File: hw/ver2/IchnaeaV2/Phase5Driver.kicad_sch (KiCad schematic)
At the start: 21 parts, among them Q2 MCAC80N10Y, Q3 MCAC80N10Y, Q4 MCAC80N10Y, Q5 MCAC80N10Y, U2 HIP2210

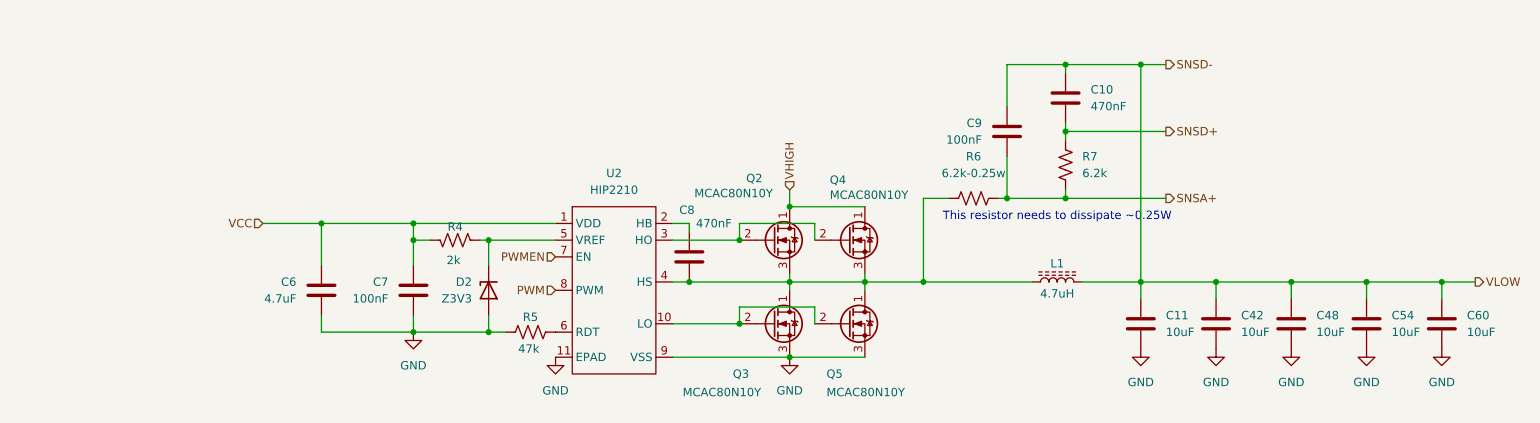
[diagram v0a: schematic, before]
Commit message: Trying to further compress power loop area
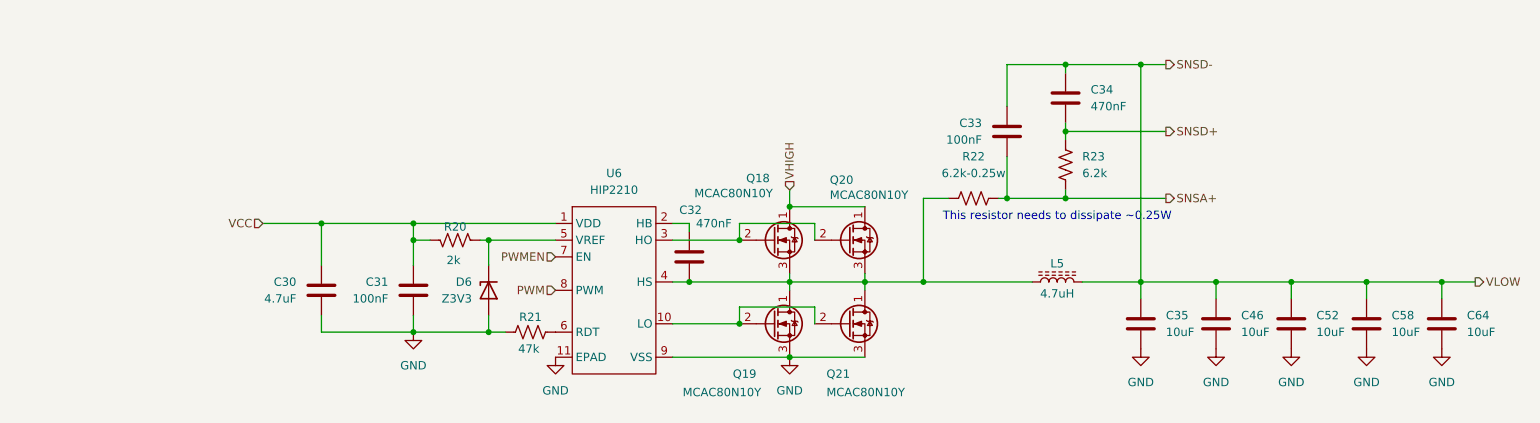
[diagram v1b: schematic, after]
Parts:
- renumbered C6 to C30, C7 to C31, C8 to C32, C9 to C33, C10 to C34, C11 to C35, C42 to C46, C48 to C52, C54 to C58, C60 to C64, D2 to D6, L1 to L5, Q2 to Q18, Q3 to Q19, Q4 to Q20, Q5 to Q21, R4 to R20, R5 to R21, R6 to R22, R7 to R23, U2 to U6

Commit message: Not quite happy with the power stage just yet.
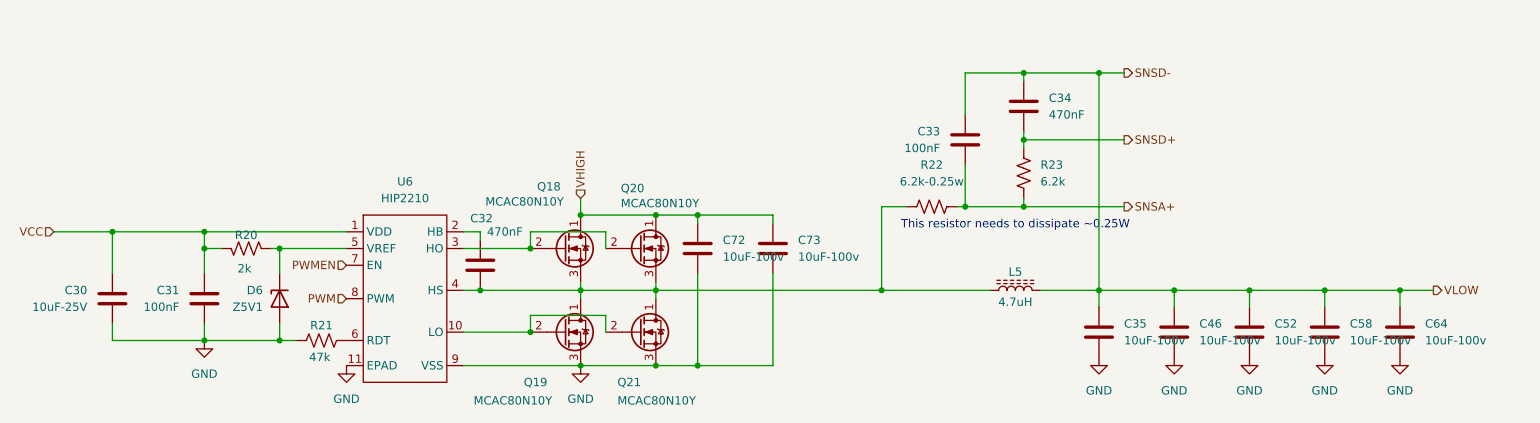
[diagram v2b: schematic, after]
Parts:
- added C72, C73: 10uF-100v, Capacitor_SMD:C_1210_3225Metric_Pad1.33x2.70mm_HandSolder, symbol Device:C
- C30: value 4.7uF -> 10uF-25V; LCSC C19666 -> C96446
- C35, C46, C52, C58, C64: value 10uF -> 10uF-100v
- D6: value Z3V3 -> Z5V1; LCSC C5353025 -> C2903912
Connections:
- net GND: now also C72.2, C73.2
- net VHIGH: now also C72.1, C73.1
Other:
- moved on the sheet: C30, C31, C32, C33, C34, C35, C46, C52, C58, C64, D6, L5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

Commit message: Sync work to main PC
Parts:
- removed C31: 100nF, Capacitor_SMD:C_0603_1608Metric, symbol Device:C
- removed D6: Z5V1, Diode_SMD:D_SOD-123, symbol Device:D_Zener
- removed R20: 2k, Resistor_SMD:R_0603_1608Metric, symbol Device:R_US
- added R62, R63: 0, Resistor_SMD:R_0603_1608Metric, symbol Device:R_US
- added R64: 10k, Resistor_SMD:R_0603_1608Metric, symbol Device:R_US
- added R65: 6.2k, Resistor_SMD:R_0603_1608Metric, symbol Device:R_US
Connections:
- net GND: now also R65.2
- net PWM: now also R63.2; no longer U6.8 (PWM)
- net PWMEN: now also R62.2; no longer U6.7 (EN)
- net SNSD-: now also L5.1; no longer L5.2
- net VCC: now also R64.1
- net at C32.2, Q18.3 (S), Q19.1 (D)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: now also L5.2; no longer L5.1
- net at U6.5 (VREF): now also R64.2, R65.1
- new net: R62.1, U6.7 (EN)
- new net: R63.1, U6.8 (PWM)
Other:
- moved on the sheet: C30, L5

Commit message: More power stage layout
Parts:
- removed C52: 10uF-100v, Capacitor_SMD:C_1210_3225Metric_Pad1.33x2.70mm_HandSolder, symbol Device:C
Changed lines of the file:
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@@
-	)
-	(junction
-		(at 232.41 96.52)
-		(diameter 0)
-		(color 0 0 0 0)
 	)
 	(junction
@@
 	(wire
 		(pts
-			(xy 232.41 96.52) (xy 232.41 99.06)
-		)
-		(stroke
-			(width 0)
-			(type default)
-		)
-	)
-	(wire
-		(pts
 			(xy 209.55 63.5) (xy 198.12 63.5)
 		)
@@
 	(wire
 		(pts
-			(xy 232.41 96.52) (xy 243.84 96.52)
+			(xy 220.98 96.52) (xy 243.84 96.52)
 		)
 		(stroke
@@
 		(pts
 			(xy 113.03 90.17) (xy 123.19 90.17)
-		)
-		(stroke
-			(width 0)
-			(type default)
-		)
-	)
-	(wire
-		(pts
-			(xy 220.98 96.52) (xy 232.41 96.52)
 		)
 		(stroke
@@
 	)
 	(symbol
-		(lib_id "Device:C")
-		(at 232.41 102.87 0)
-		(unit 1)
-		(exclude_from_sim no)
-		(in_bom yes)
-		(on_board yes)
-		(dnp no)
-		(fields_autoplaced yes)
-		(property "Reference" "C52"
-			(at 236.22 101.5999 0)
-			(effects
-				(font
-					(size 1.27 1.27)
-				)
-				(justify left)
-			)
-		)
-		(property "Value" "10uF-100v"
-			(at 236.22 104.1399 0)
-			(effects
-				(font
-					(size 1.27 1.27)
-				)
-				(justify left)
-			)
-		)
-		(property "Footprint" "Capacitor_SMD:C_1210_3225Metric_Pad1.33x2.70mm_HandSolder"
-			(at 233.3752 106.68 0)
-			(effects
-				(font
-					(size 1.27 1.27)
-				)
-				(hide yes)
-			)
-		)
-		(property "Datasheet" "~"
-			(at 232.41 102.87 0)
-			(effects
-				(font
-					(size 1.27 1.27)
-				)
-				(hide yes)
-			)
-		)
-		(property "Description" "Unpolarized capacitor"
-			(at 232.41 102.87 0)
-			(effects
-				(font
-					(size 1.27 1.27)
-				)
-				(hide yes)
-			)
-		)
-		(property "Field-1" ""
-			(at 232.41 102.87 0)
-			(effects
-				(font
-					(size 1.27 1.27)
-				)
-				(hide yes)
-			)
-		)
-		(property "Digikey" "445-CGA6P1X7R1N106M250ACCT-ND"
-			(at 232.41 102.87 0)
-			(effects
-				(font
-					(size 1.27 1.27)
-				)
-				(hide yes)
-			)
-		)
-		(property "LCSC" "C576517"
-			(at 232.41 102.87 0)
-			(effects
-				(font
-					(size 1.27 1.27)
-				)
-				(hide yes)
-			)
-		)
-		(pin "1"
-		)
-		(pin "2"
-		)
-		(instances
-			(project "IchnaeaV2"
-				(path "/93408532-1ffa-463d-873c-16289d2b7987/31a930eb-86fc-490d-aa2b-31b72c4dd29d/54a63e50-1efe-4308-b876-98aee26e8c6e"
-					(reference "C52")
-					(unit 1)
-				)
-			)
-		)
-	)
-	(symbol
 		(lib_id "Device:L_Ferrite")
 		(at 196.85 96.52 270)
@@
 					(unit 1)
 				)
-			)
-		)
-	)
-	(symbol
-		(lib_id "power:GND")
-		(at 232.41 106.68 0)
-		(unit 1)
-		(exclude_from_sim no)
-		(in_bom yes)
-		(on_board yes)
-		(dnp no)
-		(fields_autoplaced yes)
-		(property "Reference" "#PWR078"
-			(at 232.41 113.03 0)
-			(effects
-				(font
-					(size 1.27 1.27)
-				)
-				(hide yes)
-			)
-		)
-		(property "Value" "GND"
-			(at 232.41 111.76 0)
-			(effects
-				(font
-					(size 1.27 1.27)
-				)
-			)
-		)
-		(property "Footprint" ""
-			(at 232.41 106.68 0)
-			(effects
-				(font
-					(size 1.27 1.27)
-				)
-				(hide yes)
-			)
-		)
-		(property "Datasheet" ""
-			(at 232.41 106.68 0)
-			(effects
-				(font
-					(size 1.27 1.27)
-				)
-				(hide yes)
-			)
-		)
-		(property "Description" "Power symbol creates a global label with name \"GND\" , ground"
-			(at 232.41 106.68 0)
-			(effects
-				(font
-					(size 1.27 1.27)
-				)
-				(hide yes)
-			)
-		)
-		(pin "1"
-		)
-		(instances
-			(project "IchnaeaV2"
-				(path "/93408532-1ffa-463d-873c-16289d2b7987/31a930eb-86fc-490d-aa2b-31b72c4dd29d/54a63e50-1efe-4308-b876-98aee26e8c6e"
-					(reference "#PWR078")
-					(unit 1)
-				)

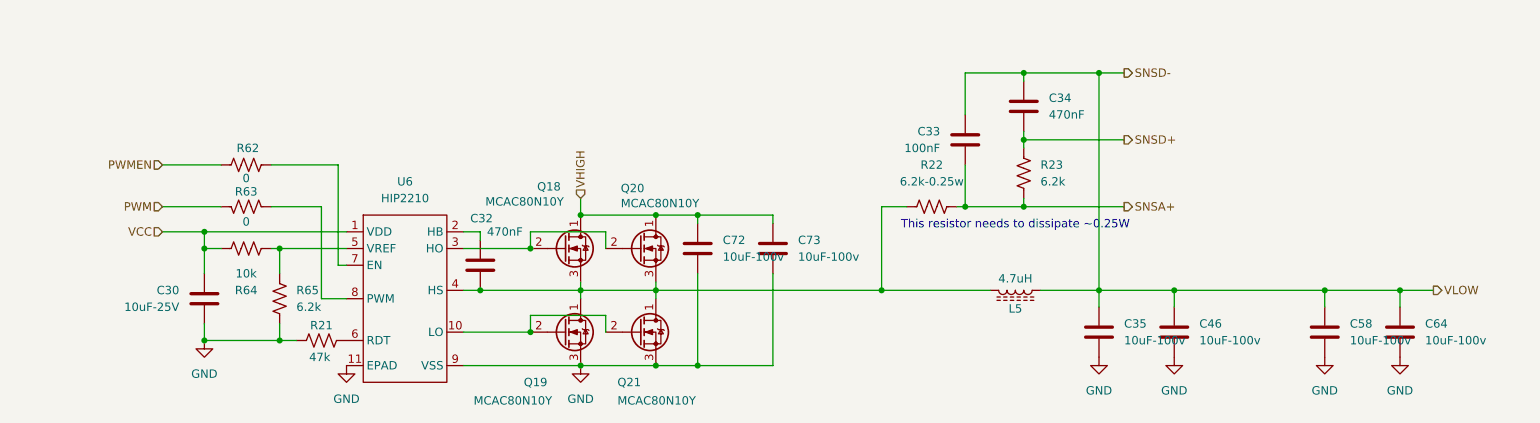
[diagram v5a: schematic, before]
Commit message: Partially work through the V1 notes. Start adding some of the control stage circuitry.
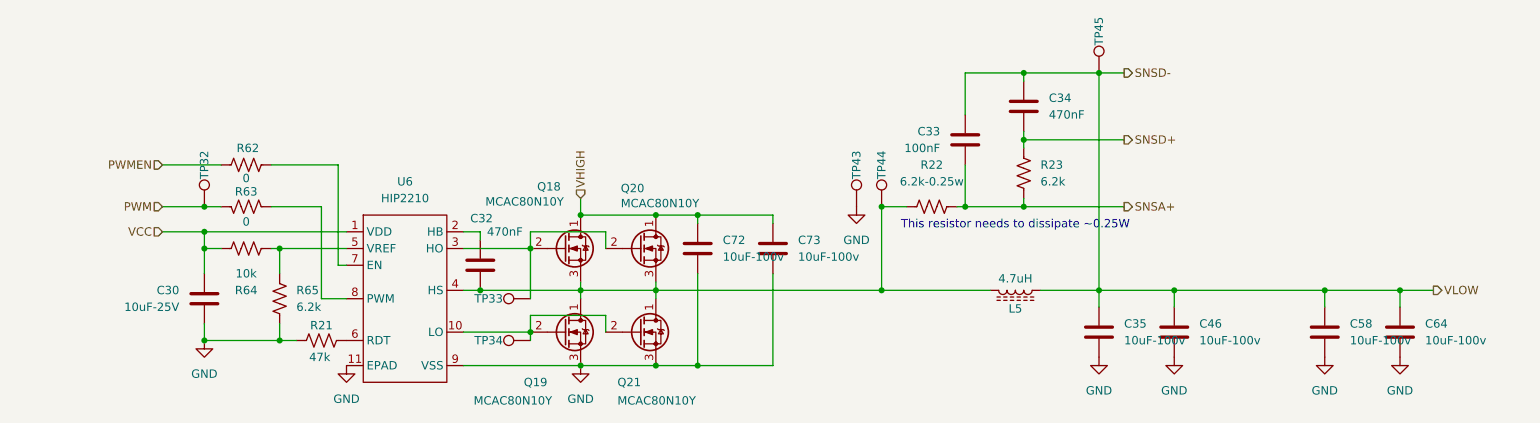
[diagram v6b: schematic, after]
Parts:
- added TP32, TP33, TP34, TP43, TP44, TP45: TestPoint, TestPoint:TestPoint_Pad_D1.0mm, symbol Connector:TestPoint
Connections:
- net GND: now also TP43.1
- net PWM: now also TP32.1
- net SNSD-: now also TP45.1
- net at C32.2, L5.2, Q18.3 (S)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: now also TP44.1
- net at Q19.2 (G), Q21.2 (G), U6.10 (LO): now also TP34.1
- net at Q18.2 (G), Q20.2 (G), U6.3 (HO): now also TP33.1

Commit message: Test production outputs for V2
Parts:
- R22: LCSC N/A -> C3017007
- TP32, TP33, TP34, TP43, TP44, TP45: LCSC (none) -> N/A
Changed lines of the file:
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@@
+			)
+		)
+		(property "LCSC" "N/A"
+			(at 172.72 83.82 0)
+			(effects
+				(font
+					(size 1.27 1.27)
+				)
+				(hide yes)
 			)
 		)
@@
 			)
 		)
+		(property "LCSC" "N/A"
+			(at 123.19 97.79 0)
+			(effects
+				(font
+					(size 1.27 1.27)
+				)
+				(hide yes)
+			)
+		)
 		(pin "1"
 		)
@@
 			)
 		)
+		(property "LCSC" "N/A"
+			(at 73.66 83.82 0)
+			(effects
+				(font
+					(size 1.27 1.27)
+				)
+				(hide yes)
+			)
+		)
 		(pin "1"
 		)
@@
 			)
 		)
+		(property "LCSC" "N/A"
+			(at 209.55 63.5 0)
+			(effects
+				(font
+					(size 1.27 1.27)
+				)
+				(hide yes)
+			)
+		)
 		(pin "1"
 		)
@@
 			)
 		)
-		(property "LCSC" "N/A"
+		(property "LCSC" "C3017007"
 			(at 184.15 83.82 0)
 			(effects
@@
 			)
 		)
+		(property "LCSC" "N/A"
+			(at 176.53 83.82 0)
+			(effects
+				(font
+					(size 1.27 1.27)
+				)
+				(hide yes)
+			)
+		)
 		(pin "1"
 		)
@@
 			(at 123.19 104.14 0)
 			(effects
+				(font
+					(size 1.27 1.27)
+				)
+				(hide yes)
+			)
+		)
+		(property "LCSC" "N/A"
+			(at 123.19 104.14 0)
+			(effects

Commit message: Sync schematic updates
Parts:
- R21: LCSC C21189 -> C25819
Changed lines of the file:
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@@
 			)
 		)
-		(property "LCSC" "C21189"
+		(property "LCSC" "C25819"
 			(at 91.44 104.14 0)
 			(effects
